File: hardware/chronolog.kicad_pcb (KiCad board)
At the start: 2 copper layers, 0 parts

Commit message: hardware(feat): import components into pcb
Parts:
- added BT1: BS-08-B2AA001, 09_electromechanical:SMD_BS-08-B2AA001, F.Cu at (235.1, 108.9)
- added C1: 47uF, 02_capacitors:CP_Elec_6.3x5.8, F.Cu at (305.0, 123.0)
- added C10: 100nF, 02_capacitors:C_0603_1608Metric, F.Cu at (253.1, 104.5)
- added C11: 4.7uF, 02_capacitors:C_0603_1608Metric, F.Cu at (253.1, 107.0)
- added C12: 1uF, 02_capacitors:C_0603_1608Metric, F.Cu at (253.1, 109.5)
- added C13: 10nF, 02_capacitors:C_0603_1608Metric, F.Cu at (253.1, 112.0)
- added C14: 100nF, 02_capacitors:C_0603_1608Metric, F.Cu at (253.1, 114.6)
- added C15: 100nF, 02_capacitors:C_0603_1608Metric, F.Cu at (257.1, 99.5)
- added C16: 10uF, 02_capacitors:C_0805_2012Metric, F.Cu at (293.7, 121.2)
- added C17: 100nF, 02_capacitors:C_0603_1608Metric, F.Cu at (283.8, 107.0)
- added C18: 100nF, 02_capacitors:C_0603_1608Metric, F.Cu at (283.8, 109.5)
- added C19: 22uF, 02_capacitors:C_0805_2012Metric, F.Cu at (293.7, 124.2)
- added C2: 10uF, 02_capacitors:C_1210_3225Metric, F.Cu at (288.7, 100.4)
- added C20: 100nF, 02_capacitors:C_0603_1608Metric, F.Cu at (257.1, 102.0)
- added C21: 18pF, 02_capacitors:C_0603_1608Metric, F.Cu at (257.1, 104.5)
- added C22: 18pF, 02_capacitors:C_0603_1608Metric, F.Cu at (257.1, 107.0)
- added C23: 100nF, 02_capacitors:C_0603_1608Metric, F.Cu at (230.4, 120.9)
- added C24: 100nF, 02_capacitors:C_0603_1608Metric, F.Cu at (305.5, 70.3)
- added C25: 100nF, 02_capacitors:C_0603_1608Metric, F.Cu at (305.5, 72.9)
- added C26: 100nF, 02_capacitors:C_0603_1608Metric, F.Cu at (305.5, 75.4)
- added C27: 100nF, 02_capacitors:C_0603_1608Metric, F.Cu at (305.5, 77.9)
- added C28: 100nF, 02_capacitors:C_0603_1608Metric, F.Cu at (321.4, 42.1)
- added C29: 10uF, 02_capacitors:C_0805_2012Metric, F.Cu at (321.7, 54.9)
- added C3: 100nF, 02_capacitors:C_0603_1608Metric, F.Cu at (283.8, 99.5)
- added C30: 100nF, 02_capacitors:C_0603_1608Metric, F.Cu at (221.9, 79.9)
- added C31: 100nF, 02_capacitors:C_0603_1608Metric, F.Cu at (221.9, 82.4)
- added C4: 100nF, 02_capacitors:C_0603_1608Metric, F.Cu at (283.8, 102.0)
- added C5: 22uF, 02_capacitors:C_1210_3225Metric, F.Cu at (288.7, 104.6)
- added C6: 22uF, 02_capacitors:C_1210_3225Metric, F.Cu at (288.7, 108.9)
- added C7: 100nF, 02_capacitors:C_0603_1608Metric, F.Cu at (283.8, 104.5)
- added C8: 100nF, 02_capacitors:C_0603_1608Metric, F.Cu at (253.1, 99.5)
- added C9: 100nF, 02_capacitors:C_0603_1608Metric, F.Cu at (253.1, 102.0)
- added D1: B340AE-13, 04_diodes:D_SMA, F.Cu at (295.7, 112.8)
- added D2: SMAJ33A, 04_diodes:D_SMA, F.Cu at (295.7, 117.4)
- added D3: KT-0603R, 04_diodes:LED_0603_1608Metric, F.Cu at (287.9, 112.3)
- added D4: KT-0603R, 04_diodes:LED_0603_1608Metric, F.Cu at (287.9, 115.0)
- added D5: XL-5050RGBC, 04_diodes:PLCC-6_XL-5050RGBC, F.Cu at (272.2, 118.0)
- added D6: B5819W-TP, 04_diodes:D_SOD-123, F.Cu at (276.0, 112.4)
- added D7: BAT54C, 04_diodes:SOT-23, F.Cu at (234.8, 122.3)
- added J1: DC-005-5A-2.0, 08_connectors:TH_DC-005-5A-2.0, F.Cu at (306.1, 103.8)
- added J2: B4B-XH-A, 08_connectors:JST_XH_B4B-XH-A_1x04_P2.50mm_Vertical, F.Cu at (266.6, 101.6)
- added J3: B-2100S04P-A110, 08_connectors:PinHeader_1x04_P2.54mm_Vertical, F.Cu at (265.4, 117.0)
- added J4: U254-051N-4BH806, 08_connectors:SMD_U254-051N-4BH806, F.Cu at (268.0, 110.7)
- added L1: 4.7uH, 03_inductors:L_1008_2520Metric, F.Cu at (288.3, 123.0)
- added Q1: BSS138, 05_transistors:SOT-23, F.Cu at (226.4, 81.3)
- added Q2: BSS138, 05_transistors:SOT-23, F.Cu at (226.4, 86.2)
- added Q3: BC817-40LT1G, 05_transistors:SOT-23, F.Cu at (226.4, 91.0)
- added R1: 10k, 01_resistors:R_0603_1608Metric, F.Cu at (257.1, 109.5)
- added R10: 100k, 01_resistors:R_0603_1608Metric, F.Cu at (283.8, 117.1)
- added R11: 22k, 01_resistors:R_0603_1608Metric, F.Cu at (283.8, 119.6)
- added R12: 10k, 01_resistors:R_0603_1608Metric, F.Cu at (230.4, 123.4)
- added R13: 10k, 01_resistors:R_0603_1608Metric, F.Cu at (305.5, 80.4)
- added R14: 10k, 01_resistors:R_0603_1608Metric, F.Cu at (305.5, 82.9)
- added R15: 10k, 01_resistors:R_0603_1608Metric, F.Cu at (305.5, 85.4)
- added R16: 4k7, 01_resistors:R_0603_1608Metric, F.Cu at (221.9, 84.9)
- added R17: 4k7, 01_resistors:R_0603_1608Metric, F.Cu at (221.9, 87.5)
- added R18: 10k, 01_resistors:R_0603_1608Metric, F.Cu at (321.4, 44.6)
- added R19: 10k, 01_resistors:R_0603_1608Metric, F.Cu at (321.4, 47.1)
- added R2: 10k, 01_resistors:R_0603_1608Metric, F.Cu at (257.1, 112.0)
- added R20: 10k, 01_resistors:R_0603_1608Metric, F.Cu at (321.4, 49.6)
- added R21: 10k, 01_resistors:R_0603_1608Metric, F.Cu at (321.4, 52.1)
- added R22: 4k7, 01_resistors:R_0603_1608Metric, F.Cu at (221.9, 90.0)
- added R23: 1k, 01_resistors:R_0603_1608Metric, F.Cu at (221.9, 92.5)
- added R24: 10k, 01_resistors:TH_3362P, F.Cu at (246.4, 82.9)
- added R25: 4k7, 01_resistors:R_0603_1608Metric, F.Cu at (221.9, 95.0)
- added R26: 12R, 01_resistors:R_0805_2012Metric, F.Cu at (244.0, 89.0)
- added R3: 0R, 01_resistors:R_0603_1608Metric, F.Cu at (257.1, 114.6)
- added R4: 4k7, 01_resistors:R_0603_1608Metric, F.Cu at (261.1, 99.5)
- added R5: 1k, 01_resistors:R_0603_1608Metric, F.Cu at (283.8, 112.0)
- added R6: 470R, 01_resistors:R_0603_1608Metric, F.Cu at (283.8, 114.6)
- added R7: 220R, 01_resistors:R_0603_1608Metric, F.Cu at (261.1, 102.0)
- added R8: 47R, 01_resistors:R_0603_1608Metric, F.Cu at (261.1, 104.5)
- added R9: 47R, 01_resistors:R_0603_1608Metric, F.Cu at (261.1, 107.0)
- added S1: TS-1088-AR02016, 09_electromechanical:SW_SPST_TS-1088-xR020, F.Cu at (271.2, 123.6)
- added S2: TS-1088-AR02016, 09_electromechanical:SW_SPST_TS-1088-xR020, F.Cu at (311.0, 71.4)
- added S3: TS-1088-AR02016, 09_electromechanical:SW_SPST_TS-1088-xR020, F.Cu at (311.0, 75.9)
- added S4: TS-1088-AR02016, 09_electromechanical:SW_SPST_TS-1088-xR020, F.Cu at (311.0, 80.5)
- added TP1: 1.0P-SMD, 12_mechanical:TestPoint_Pad_D1.0mm, F.Cu at (277.9, 116.3)
- added U1: AP63205WU-7, 06_ics:TSOT-23-6, F.Cu at (288.4, 118.9)
- added U2: STM32F072CBT6, 06_ics:LQFP-48_7x7mm_P0.5mm, F.Cu at (256.8, 121.5)
- added U3: AP2114H-3.3TRG1, 06_ics:SOT-223-3_TabPin2, F.Cu at (304.7, 114.8)
- added U4: USBLC6-2SC6, 06_ics:SOT-23-6, F.Cu at (275.5, 108.5)
- added U5: W25Q32JVSNIQ, 06_ics:SOIC-8_3.9x4.9mm_P1.27mm, F.Cu at (224.2, 123.2)
- added U6: LM75BD, 06_ics:SOIC-8_3.9x4.9mm_P1.27mm, F.Cu at (318.8, 72.6)
- added U7: ESP-01, 11_modules:ESP-01, F.Cu at (307.8, 62.3)
- added U8: WC1602A, 11_modules:WC1602A, F.Cu at (228.7, 44.4)
- added U9: PCF8574T, 06_ics:SOIC-16W_7.5x10.3mm_P1.27mm, F.Cu at (235.3, 84.7)
- added Y1: 32.768kHz, 07_crystals:Crystal_SMD_3215-2Pin_3.2x1.5mm, F.Cu at (277.3, 123.0)

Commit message: hardware(feat): add mounting holes and fiducials
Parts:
- added FID1: 1.0P-2.0M, 12_mechanical:Fiducial_1mm_Mask2mm, F.Cu at (337.4, 105.3)
- added FID2: 1.0P-2.0M, 12_mechanical:Fiducial_1mm_Mask2mm, F.Cu at (337.4, 108.9)
- added FID3: 1.0P-2.0M, 12_mechanical:Fiducial_1mm_Mask2mm, F.Cu at (337.4, 112.5)
- added FID4: 1.0P-2.0M, 12_mechanical:Fiducial_1mm_Mask2mm, F.Cu at (337.4, 116.0)
- added H1: M4-4.3D-8.6P, 12_mechanical:MountingHole_4.3mm_M4_Pad, F.Cu at (326.0, 97.5)
- added H2: M4-4.3D-8.6P, 12_mechanical:MountingHole_4.3mm_M4_Pad, F.Cu at (326.0, 107.7)
- added H3: M4-4.3D-8.6P, 12_mechanical:MountingHole_4.3mm_M4_Pad, F.Cu at (326.0, 117.8)
- added H4: M4-4.3D-8.6P, 12_mechanical:MountingHole_4.3mm_M4_Pad, F.Cu at (326.0, 128.0)

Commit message: hardware(feat): define first board shape and circuit regions
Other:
- board outline added: 120 x 90 mm
- board text added: "BUTTONS + TEMP SENSOR (LM75)"
- board text added: "DC SUPPLY 5V + LDO 3V3 (AP63205 / AP2114)"
- board text added: "ESP-01 (WI-FI)"
- board text added: "LCD 16x2 (WC1602A)"
- board text added: "LCD DRIVER (PCF8574)"
- board text added: "MCU STM32 + USB + SWD/UART + LED"
- board text added: "RTC + NOR FLASH (BT1 / W25Q32)"

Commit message: hardware(feat): place power supply components
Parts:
- moved FID1 246.2 mm to (93.5, 71.5)
- moved FID3 245.3 mm to (93.5, 138.5)
- moved H1 234.8 mm to (93.5, 65.0)
- moved H3 234.1 mm to (93.5, 145.0)
- moved J1 205.5 mm to (102.2, 78.5)
- moved C1 203.5 mm to (109.4, 66.6), turned to -90 degrees
- moved D1 192.4 mm to (106.8, 76.5), turned to -90 degrees
- moved D2 189.4 mm to (110.8, 76.5), turned to -90 degrees
- moved U3 188.9 mm to (118.5, 82.9), turned to -90 degrees
- moved C16 183.1 mm to (116.5, 75.2)
- moved C6 175.9 mm to (117.0, 70.9), turned to 90 degrees
- moved C2 173.8 mm to (118.5, 65.2), turned to -90 degrees
- moved C7 173.0 mm to (114.2, 70.6), turned to 90 degrees
- moved C19 173.0 mm to (125.2, 85.2), turned to 90 degrees
- moved U1 172.4 mm to (124.2, 66.4), turned to -90 degrees
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
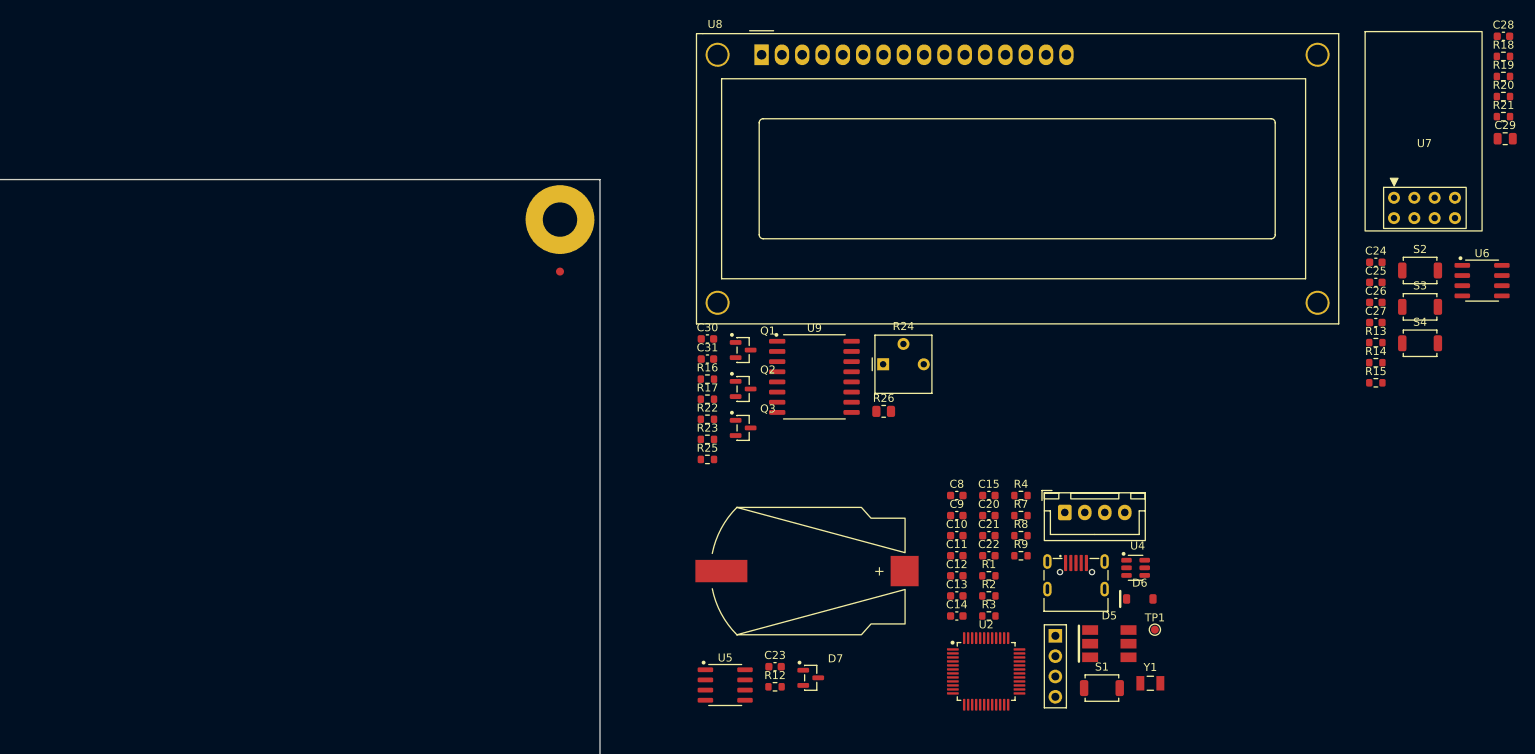
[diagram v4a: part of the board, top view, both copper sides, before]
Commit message: hardware(feat): place esp-01, rtc and nor memory
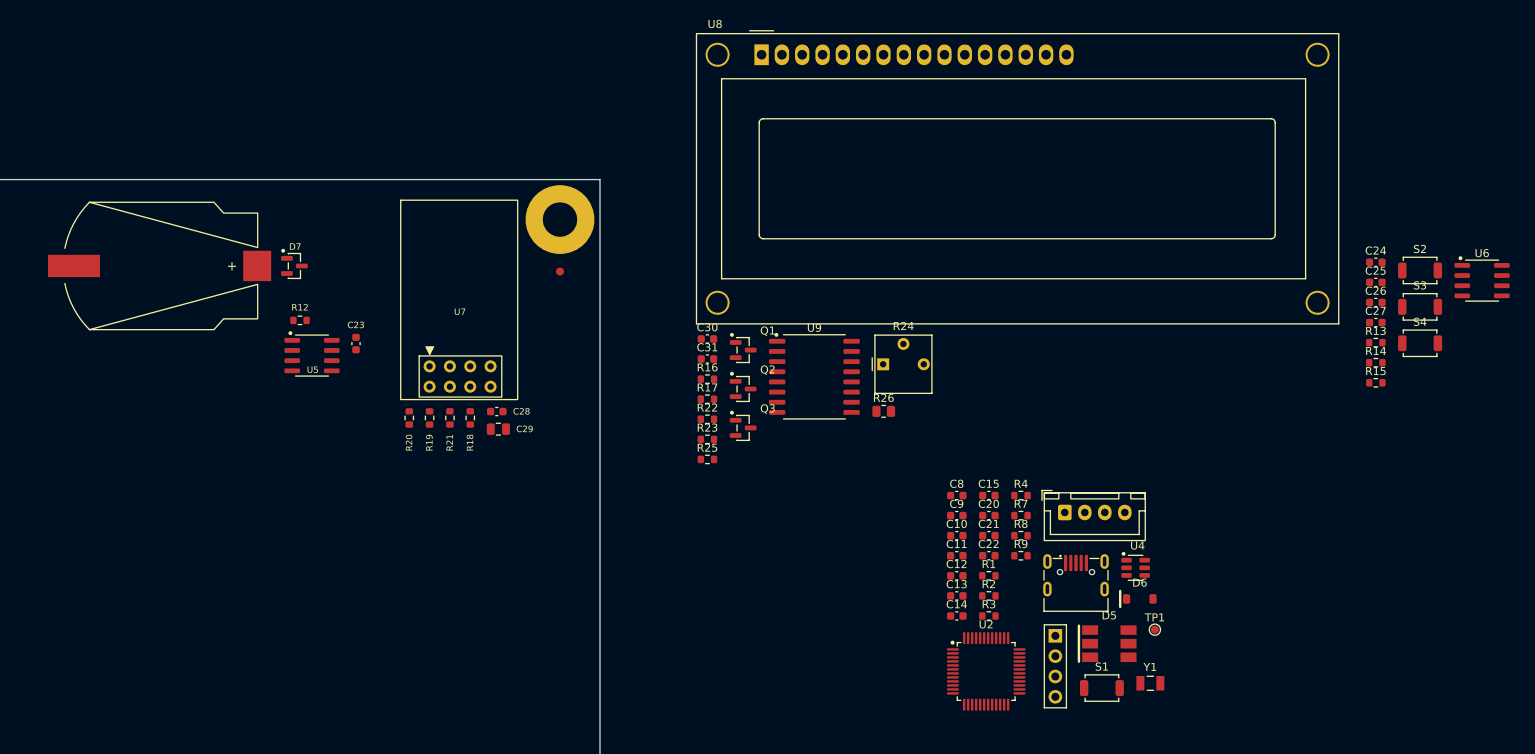
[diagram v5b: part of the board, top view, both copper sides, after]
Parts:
- moved R20 142.5 mm to (184.7, 89.8), turned to 90 degrees
- moved R19 140.9 mm to (187.2, 89.8), turned to 90 degrees
- moved R21 137.0 mm to (189.7, 89.8), turned to -90 degrees
- moved R18 136.8 mm to (192.3, 89.8), turned to 90 degrees
- moved C28 134.3 mm to (195.6, 89.0)
- moved C29 131.0 mm to (195.8, 91.2)
- moved U7 122.4 mm to (187.2, 83.3)
- moved BT1 89.5 mm to (154.2, 70.8)
- moved D7 82.6 mm to (170.3, 70.8)
- moved R12 75.0 mm to (171.0, 77.6), turned to 180 degrees
- moved C23 66.1 mm to (178.0, 80.5), turned to -90 degrees
- moved U5 66.1 mm to (172.5, 82.0)

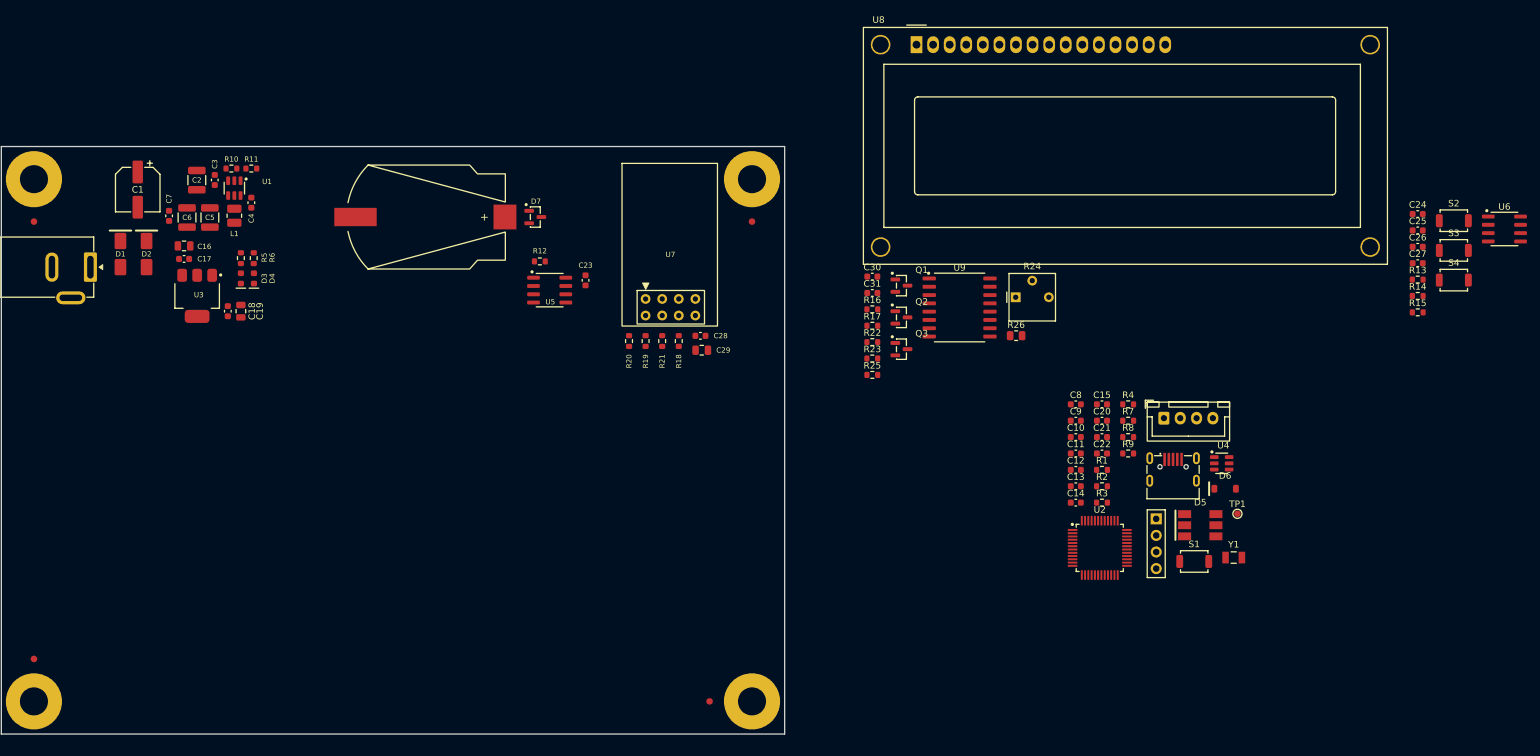
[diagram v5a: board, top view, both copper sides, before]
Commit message: hardware(feat): place lcd, lcd driver, mcu, usb, led, buttons and temp sensor
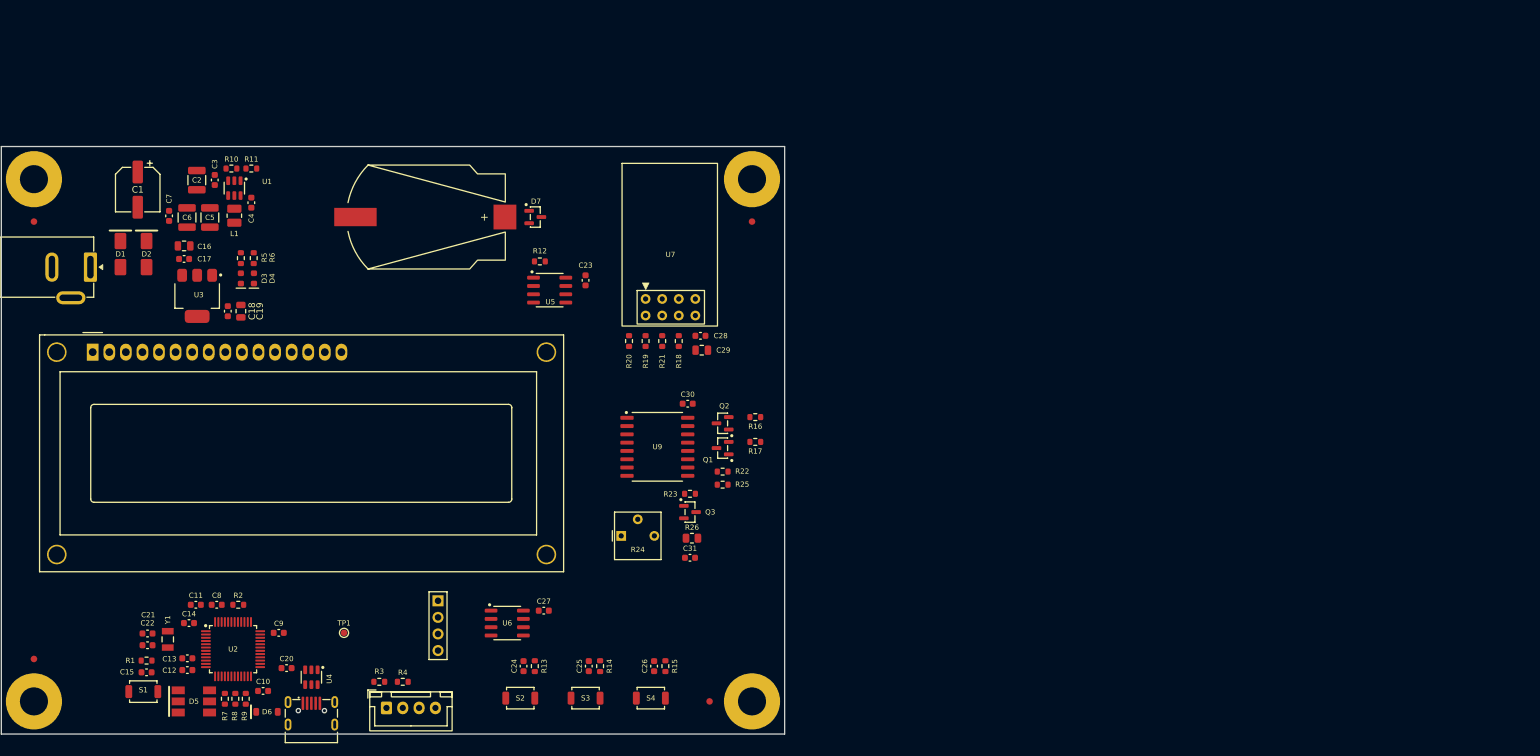
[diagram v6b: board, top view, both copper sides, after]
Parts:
- moved U6 164.3 mm to (166.0, 133.0)
- moved Y1 163.8 mm to (114.0, 135.5), turned to 90 degrees
- moved S1 162.2 mm to (110.2, 143.5)
- moved S2 160.6 mm to (168.0, 144.5)
- moved D5 156.5 mm to (118.0, 145.0)
- moved C24 153.5 mm to (168.5, 139.6), turned to 90 degrees
- moved C15 152.0 mm to (110.8, 140.6)
- moved D6 150.7 mm to (129.2, 146.6)
- moved S3 149.7 mm to (178.0, 144.5)
- moved C21 149.3 mm to (110.9, 134.6)
- moved R1 149.2 mm to (110.8, 138.8)
- moved C22 149.1 mm to (110.9, 136.4)
- moved R13 147.6 mm to (170.2, 139.6), turned to -90 degrees
- moved R7 144.8 mm to (122.8, 144.6), turned to -90 degrees
- moved C27 144.1 mm to (171.6, 131.1)
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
